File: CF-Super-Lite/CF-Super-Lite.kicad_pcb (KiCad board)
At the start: 2 copper layers, 99.9 x 99.9 mm, 6 parts, among them J1 Bus_ISA_8bit, J2 IDE_CONNECTOR

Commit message: Add IC's to schematic and PCB.
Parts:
- added U1: BIOS FLASH, Package_DIP:DIP-32_W15.24mm_Socket, F.Cu at (111.8, 104.1)
- added U2: 74HCT245, Package_DIP:DIP-20_W7.62mm_Socket, F.Cu at (134.6, 121.9)
- added U3: GAL16V8, Package_DIP:DIP-20_W7.62mm_Socket, F.Cu at (104.1, 121.9)

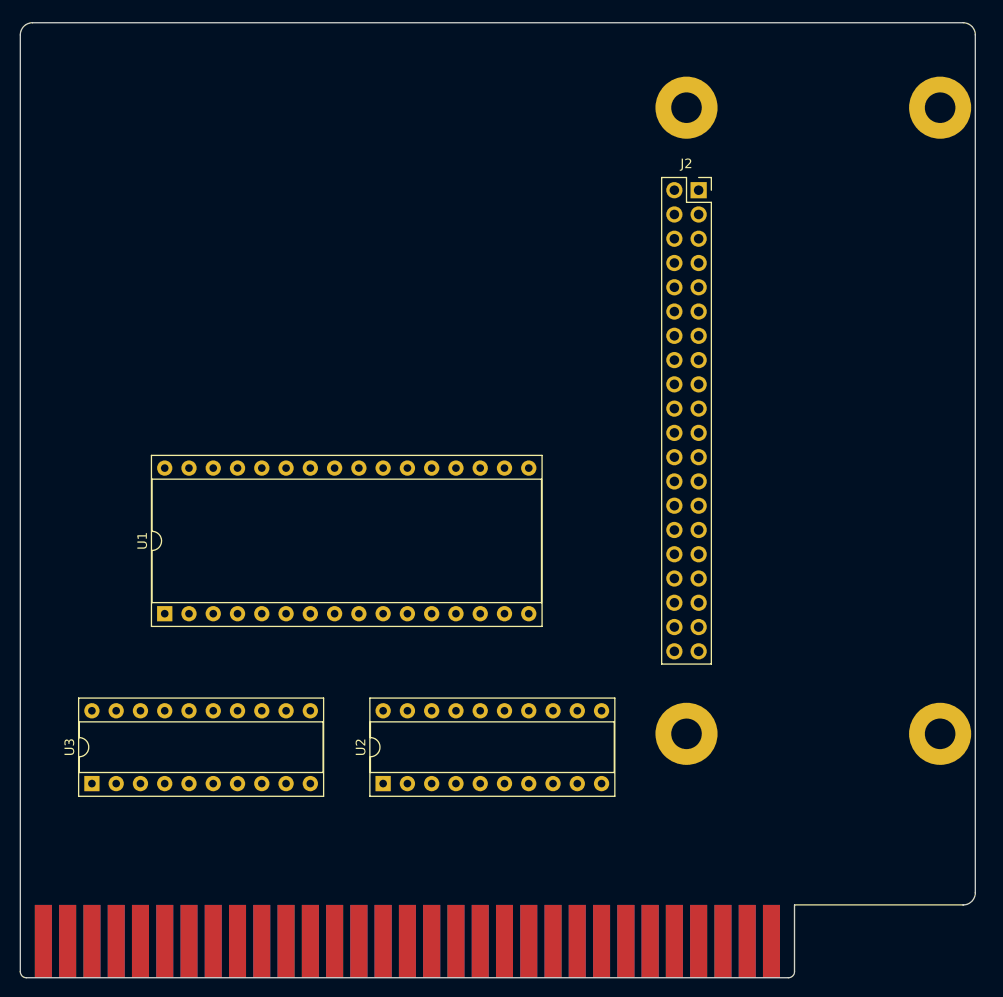
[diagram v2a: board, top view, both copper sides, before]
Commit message: Add jumper section, tidy up schematic some more.
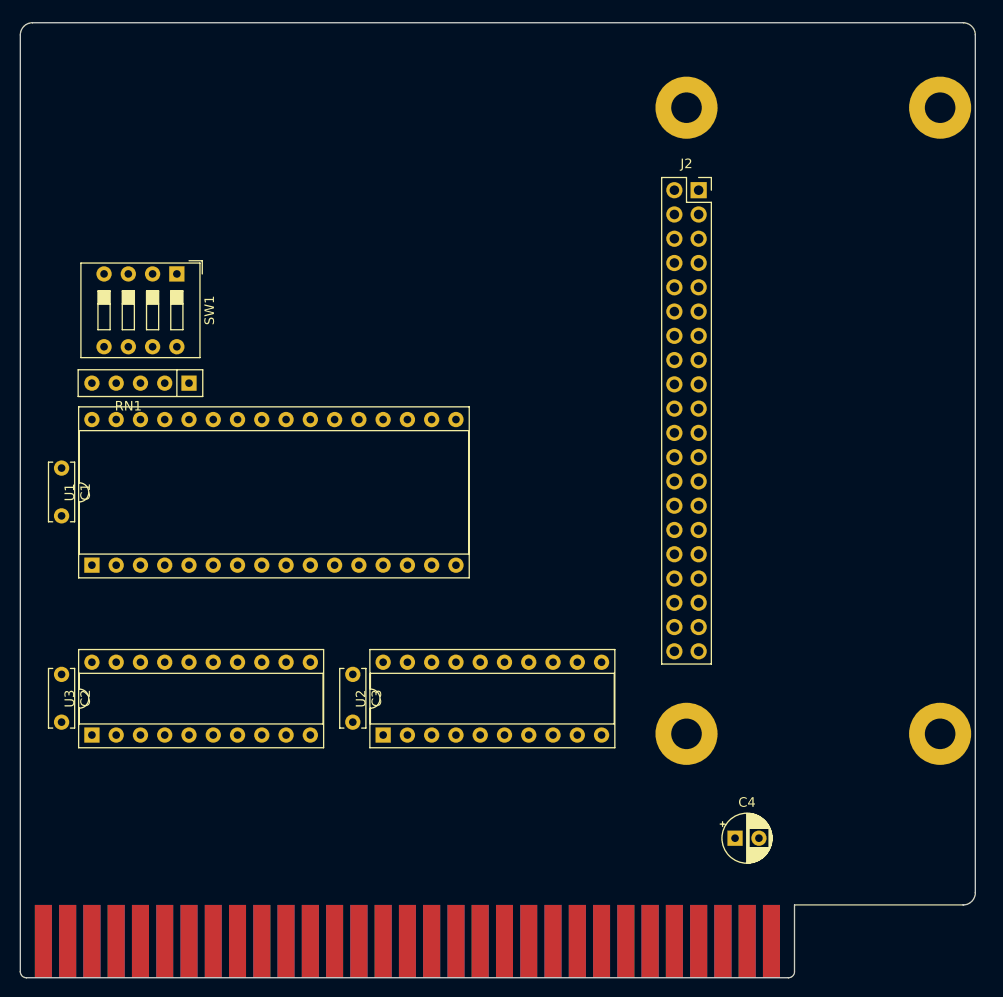
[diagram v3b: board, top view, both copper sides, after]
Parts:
- added C1: 0.1uF, Capacitor_THT:C_Disc_D6.0mm_W2.5mm_P5.00mm, F.Cu at (101.0, 88.9)
- added C2: 0.1uF, Capacitor_THT:C_Disc_D6.0mm_W2.5mm_P5.00mm, F.Cu at (101.0, 110.5)
- added C3: 0.1uF, Capacitor_THT:C_Disc_D6.0mm_W2.5mm_P5.00mm, F.Cu at (131.4, 110.5)
- added C4: 22uF, Capacitor_THT:CP_Radial_D5.0mm_P2.50mm, F.Cu at (171.4, 127.6)
- added RN1: 10K, Resistor_THT:R_Array_SIP5, F.Cu at (114.3, 80.0)
- added SW1: DIP Switch x3 or x4, Button_Switch_THT:SW_DIP_SPSTx04_Slide_9.78x12.34mm_W7.62mm_P2.54mm, F.Cu at (113.0, 68.6)
- J2: value IDE_CONNECTOR -> ATA_CONNECTOR
- moved U1 9.16 mm to (104.1, 99.1)
- moved U2 5.08 mm to (134.6, 116.8)
- moved U3 5.08 mm to (104.1, 116.8)
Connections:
- net Net-(J2-Pad1) renamed ~RESET
- net Net-(J2-Pad33) renamed A1
- net Net-(J2-Pad35) renamed A0
- net Net-(J2-Pad36) renamed A2
- J2 pad 11: Net-(J2-Pad11) -> D3_BUF
- J2 pad 13: Net-(J2-Pad13) -> D2_BUF
- J2 pad 15: Net-(J2-Pad15) -> D1_BUF
- J2 pad 17: Net-(J2-Pad17) -> D0_BUF
- J2 pad 19: Net-(J2-Pad19) -> GND
- J2 pad 2: Net-(J2-Pad2) -> GND
- J2 pad 22: Net-(J2-Pad22) -> GND
- J2 pad 23: Net-(J2-Pad23) -> ~IOW
- J2 pad 24: Net-(J2-Pad24) -> GND
- J2 pad 25: Net-(J2-Pad25) -> ~IOR
- J2 pad 26: Net-(J2-Pad26) -> GND
- J2 pad 28: Net-(J2-Pad28) -> GND
- J2 pad 3: Net-(J2-Pad3) -> D7_BUF
- J2 pad 30: Net-(J2-Pad30) -> GND
- J2 pad 37: Net-(J2-Pad37) -> ~CS0~_ATA
- J2 pad 38: Net-(J2-Pad38) -> ~CS1~_ATA
- J2 pad 40: Net-(J2-Pad40) -> GND
- J2 pad 5: Net-(J2-Pad5) -> D6_BUF
- J2 pad 7: Net-(J2-Pad7) -> D5_BUF
- J2 pad 9: Net-(J2-Pad9) -> D4_BUF
- U1 pad 1: Net-(U1-Pad1) -> GND
- U1 pad 10: Net-(U1-Pad10) -> A02
- U1 pad 11: Net-(U1-Pad11) -> A01
- U1 pad 12: Net-(U1-Pad12) -> A00
- U1 pad 13: Net-(U1-Pad13) -> D0_BUF
- U1 pad 14: Net-(U1-Pad14) -> D1_BUF
- U1 pad 15: Net-(U1-Pad15) -> D2_BUF
- U1 pad 17: Net-(U1-Pad17) -> D3_BUF
- U1 pad 18: Net-(U1-Pad18) -> D4_BUF
- U1 pad 19: Net-(U1-Pad19) -> D5_BUF
- U1 pad 2: Net-(U1-Pad2) -> GND
- U1 pad 20: Net-(U1-Pad20) -> D6_BUF
- U1 pad 21: Net-(U1-Pad21) -> D7_BUF
- U1 pad 22: Net-(U1-Pad22) -> ~CE~_BIOS
- U1 pad 23: Net-(U1-Pad23) -> A10
- U1 pad 24: Net-(U1-Pad24) -> ~MEMR
- U1 pad 25: Net-(U1-Pad25) -> A11
- U1 pad 26: Net-(U1-Pad26) -> A09
- U1 pad 27: Net-(U1-Pad27) -> A08
- U1 pad 28: Net-(U1-Pad28) -> A13
- U1 pad 29: Net-(U1-Pad29) -> ATA_ADDR_JUMPER
- U1 pad 3: Net-(U1-Pad3) -> V20_JUMPER
- U1 pad 30: Net-(U1-Pad30) -> GND
- U1 pad 31: Net-(U1-Pad31) -> ~MEMW
- U1 pad 4: Net-(U1-Pad4) -> A12
- U1 pad 5: Net-(U1-Pad5) -> A07
- U1 pad 6: Net-(U1-Pad6) -> A06
- U1 pad 7: Net-(U1-Pad7) -> A05
- U1 pad 8: Net-(U1-Pad8) -> A04
- U1 pad 9: Net-(U1-Pad9) -> A03
- U2 pad 1: Net-(U2-Pad1) -> ~IOR
- U2 pad 10: Net-(U2-Pad10) -> GND
- U2 pad 11: Net-(U2-Pad11) -> D7_BUF
- U2 pad 12: Net-(U2-Pad12) -> D6_BUF
- U2 pad 13: Net-(U2-Pad13) -> D5_BUF
- U2 pad 14: Net-(U2-Pad14) -> D4_BUF
- U2 pad 15: Net-(U2-Pad15) -> D3_BUF
- U2 pad 16: Net-(U2-Pad16) -> D2_BUF
- U2 pad 17: Net-(U2-Pad17) -> D1_BUF
- U2 pad 18: Net-(U2-Pad18) -> D0_BUF
- U2 pad 19: Net-(U2-Pad19) -> ~CE~_D_BUF
- U2 pad 2: Net-(U2-Pad2) -> D0
- U2 pad 20: Net-(U2-Pad20) -> VCC
- U2 pad 3: Net-(U2-Pad3) -> D1
- U2 pad 4: Net-(U2-Pad4) -> D2
- U2 pad 5: Net-(U2-Pad5) -> D3
- U2 pad 6: Net-(U2-Pad6) -> D4
- U2 pad 7: Net-(U2-Pad7) -> D5
- U2 pad 8: Net-(U2-Pad8) -> D6
- U2 pad 9: Net-(U2-Pad9) -> D7
- U3 pad 1: Net-(U3-Pad1) -> A04
- U3 pad 10: Net-(U3-Pad10) -> GND
- U3 pad 11: Net-(U3-Pad11) -> A17
- U3 pad 12: Net-(U3-Pad12) -> A19
- U3 pad 13: Net-(U3-Pad13) -> A18
- U3 pad 14: Net-(U3-Pad14) -> ATA_ADDR_JUMPER
- U3 pad 15: Net-(U3-Pad15) -> ROM_ADDR_JUMPER
- U3 pad 16: Net-(U3-Pad16) -> ~CE~_D_BUF
- U3 pad 17: Net-(U3-Pad17) -> ~CE~_BIOS
- U3 pad 18: Net-(U3-Pad18) -> ~CS1~_ATA
- U3 pad 19: Net-(U3-Pad19) -> ~CS0~_ATA
- U3 pad 2: Net-(U3-Pad2) -> A05
- U3 pad 20: Net-(U3-Pad20) -> VCC
- U3 pad 3: Net-(U3-Pad3) -> A06
- U3 pad 4: Net-(U3-Pad4) -> A07
- U3 pad 5: Net-(U3-Pad5) -> A08
- U3 pad 6: Net-(U3-Pad6) -> A09
- U3 pad 7: Net-(U3-Pad7) -> A14
- U3 pad 8: Net-(U3-Pad8) -> A15
- U3 pad 9: Net-(U3-Pad9) -> A16
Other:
- net class Default: clearance 0.2 -> 0.25; trace_width 0.25 -> 0.35
- net class Power added: clearance 0.25, trace_width 0.5, via_dia 1, via_drill 0.6
- rule trace_clearance: 0.2 -> 0.25

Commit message: CF-Super-Lite: Added a bunch of premature layout.
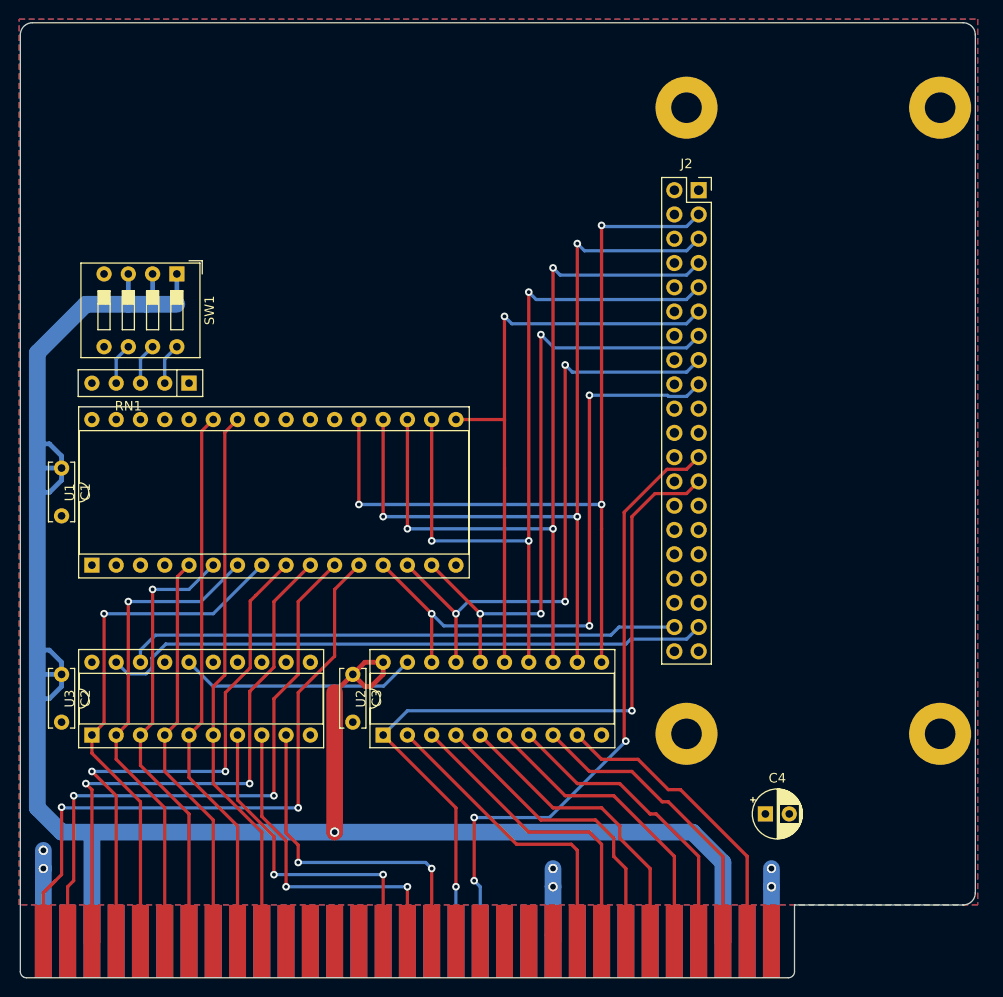
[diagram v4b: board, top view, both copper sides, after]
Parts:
- moved C4 4.07 mm to (174.6, 125.1)
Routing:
- net VCC: track 0.00 -> 216.9 mm, vias 0 -> 1
- net D7_BUF: track 0.00 -> 90.7 mm, vias 0 -> 3
- net D6_BUF: track 0.00 -> 87.8 mm, vias 0 -> 3
- net D5_BUF: track 0.00 -> 84.0 mm, vias 0 -> 3
- net ~IOR: track 0.00 -> 80.7 mm, vias 0 -> 2
- net D4_BUF: track 0.00 -> 80.2 mm, vias 0 -> 3
- net A00: track 0.00 -> 69.4 mm, vias 0 -> 2
- net ~IOW: track 0.00 -> 66.6 mm, vias 0 -> 3
- net D2_BUF: track 0.00 -> 65.4 mm, vias 0 -> 3
- net D0_BUF: track 0.00 -> 65.4 mm, vias 0 -> 3
- net ~CS0~_ATA: track 0.00 -> 64.1 mm
- net D1_BUF: track 0.00 -> 63.8 mm, vias 0 -> 3
- net A01: track 0.00 -> 63.2 mm, vias 0 -> 2
- net D3_BUF: track 0.00 -> 62.4 mm, vias 0 -> 1
- net A02: track 0.00 -> 59.4 mm, vias 0 -> 2
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- added copper zone on B.Cu, net GND
- added copper zone on F.Cu, net GND
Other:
- net class Default: clearance 0.25 -> 0.24; trace_width 0.35 -> 0.34
- rule trace_clearance: 0.25 -> 0.24

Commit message: More premature layout work.
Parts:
- moved SW1 3.81 mm to (113.0, 72.4)
- moved U1 3.81 mm to (104.1, 102.9)
- moved RN1 3.81 mm to (114.3, 83.8)
- moved C1 1.27 mm to (101.0, 87.6)
- moved U2 1.27 mm to (134.6, 118.1)
- moved U3 1.27 mm to (104.1, 118.1)
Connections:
- MH1 pad : (no net) -> GND
- MH2 pad : (no net) -> GND
- MH3 pad : (no net) -> GND
- MH4 pad : (no net) -> GND
- U3 pad 14: ATA_ADDR_JUMPER -> ~CE~_BIOS
- U3 pad 15: ROM_ADDR_JUMPER -> ~CE~_D_BUF
- U3 pad 16: ~CE~_D_BUF -> ~CS1~_ATA
- U3 pad 17: ~CE~_BIOS -> ~CS0~_ATA
- U3 pad 18: ~CS1~_ATA -> ROM_ADDR_JUMPER
- U3 pad 19: ~CS0~_ATA -> ATA_ADDR_JUMPER
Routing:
- net GND: track 24.8 -> 209.7 mm, vias 6 -> 19
- net VCC: track 216.9 -> 366.4 mm, vias 1 -> 5
- net ~MEMW: track 0.00 -> 112.1 mm, vias 0 -> 5
- net A10: track 0.00 -> 94.0 mm, vias 0 -> 2
- net A11: track 0.00 -> 73.8 mm, vias 0 -> 2
- net A13: track 0.00 -> 72.1 mm, vias 0 -> 2
- net ~MEMR: track 0.00 -> 67.7 mm, vias 0 -> 1
- net A12: track 0.00 -> 57.1 mm, vias 0 -> 4
- net A19: track 0.00 -> 46.4 mm, vias 0 -> 2
- net A18: track 0.00 -> 45.7 mm, vias 0 -> 2
- net A17: track 0.00 -> 44.9 mm, vias 0 -> 4
- net ~CE~_BIOS: track 0.00 -> 32.3 mm, vias 0 -> 2
- net ATA_ADDR_JUMPER: track 4.34 -> 35.4 mm
- net ROM_ADDR_JUMPER: track 4.34 -> 33.2 mm
- net ~IOW: track 66.6 -> 90.3 mm
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
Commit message: Add power for CF adapter to Template and CF-Super-Lite.
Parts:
- added J2: CF Adapter Power, Connector_PinHeader_2.54mm:PinHeader_1x02_P2.54mm_Vertical, F.Cu at (174.3, 59.8)
- J1: renamed from J2; value ATA_CONNECTOR -> IDE_CONNECTOR
- renumbered J1 to J3
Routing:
- net VCC: track 366.4 -> 457.1 mm, vias 5 -> 7
- net GND: track 209.7 -> 196.4 mm

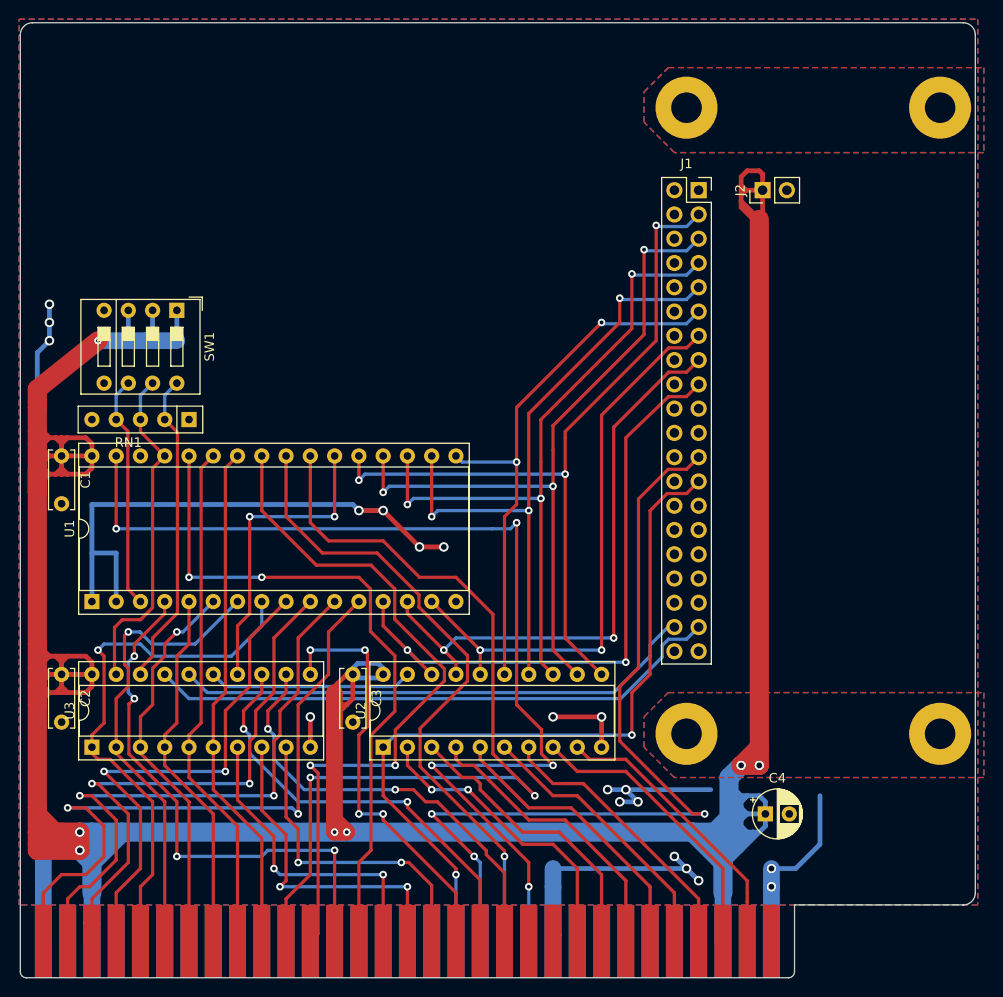
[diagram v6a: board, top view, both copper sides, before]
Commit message: Finish remaining IDE signal directions based on the ATA spec rev 1. Correct IDE address assignments and route the new connections on the PCB.
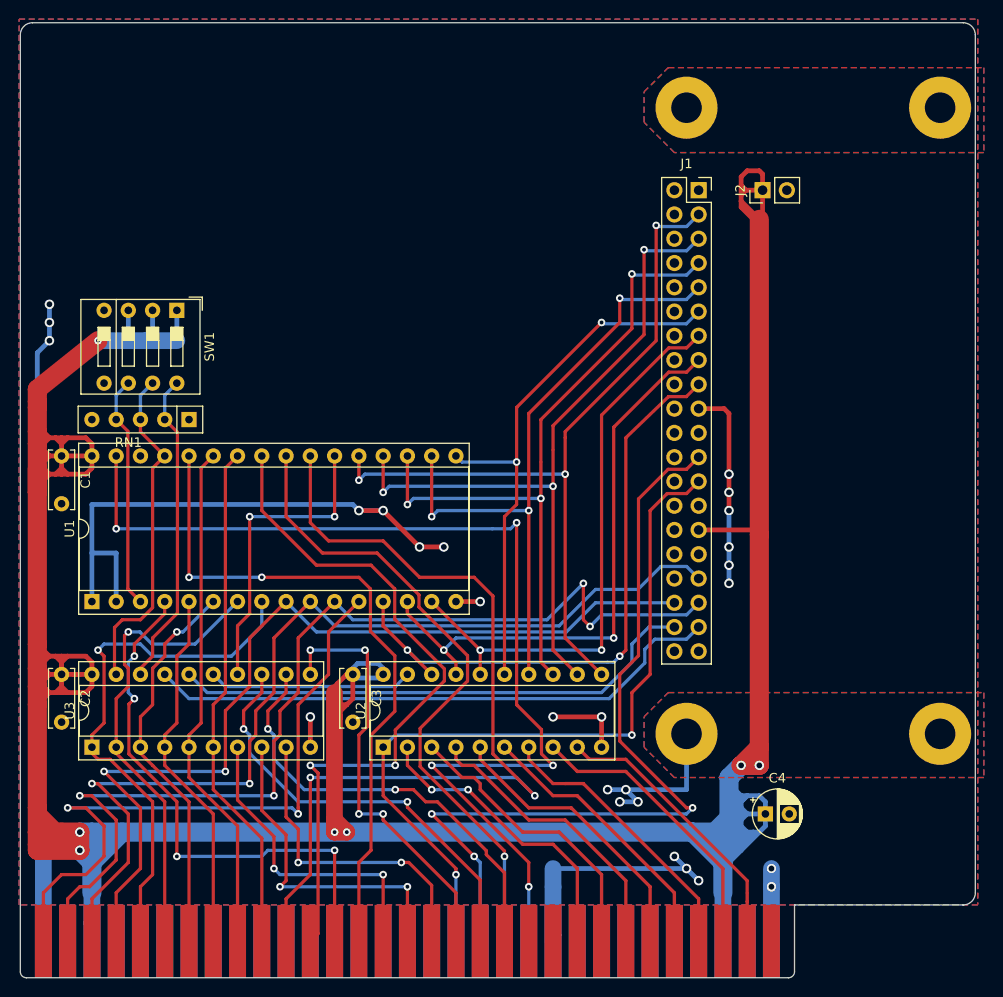
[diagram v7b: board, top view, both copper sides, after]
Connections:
- J1 pad 29: Net-(J1-Pad29) -> VCC
- J1 pad 33: A1 -> A02
- J1 pad 35: A0 -> A01
- J1 pad 36: A2 -> A03
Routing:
- net A01: track 63.5 -> 109.1 mm, vias 2 -> 4
- net A02: track 58.2 -> 103.0 mm
- net A03: track 53.5 -> 96.7 mm
- net GND: track 196.4 -> 212.2 mm, vias 19 -> 26
- net VCC: track 457.1 -> 463.6 mm
- net ~IOW: track 90.3 -> 87.8 mm
- net A10: track 94.0 -> 95.1 mm
- net D0_BUF: track 66.5 -> 65.7 mm

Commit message: Final updates before trying to resolve unimplemented reset inversion.
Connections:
- net +12V renamed Net-(J3-Pad9)
- net -12V renamed Net-(J3-Pad7)
- net -5V renamed Net-(J3-Pad5)
- net AEN renamed Net-(J3-Pad42)
- net ALE renamed Net-(J3-Pad28)
- net CLK renamed Net-(J3-Pad20)
- net DRQ1 renamed Net-(J3-Pad18)
- net DRQ2 renamed Net-(J3-Pad6)
- net DRQ3 renamed Net-(J3-Pad16)
- net IOCHRDY renamed Net-(J3-Pad41)
- net IRQ2 renamed Net-(J3-Pad4)
- net IRQ3 renamed Net-(J3-Pad25)
- net IRQ4 renamed Net-(J3-Pad24)
- net IRQ5 renamed Net-(J3-Pad23)
- net IRQ6 renamed Net-(J3-Pad22)
- net IRQ7 renamed Net-(J3-Pad21)
- net OSC renamed Net-(J3-Pad30)
- net TC renamed Net-(J3-Pad27)
- net ~DACK0 renamed Net-(J3-Pad19)
- net ~DACK1 renamed Net-(J3-Pad17)
- net ~DACK2 renamed Net-(J3-Pad26)
- net ~DACK3 renamed Net-(J3-Pad15)
- net ~IO_CH_CK renamed Net-(J3-Pad32)
- J1 pad 28: GND -> Net-(J1-Pad28)
